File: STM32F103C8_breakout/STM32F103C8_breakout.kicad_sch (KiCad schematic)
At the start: 51 parts, among them J1 Conn1x1Pin-PA0_WKUP, J10 Conn1x1Pin-PA9, J11 Conn1x1Pin-PA10, J12 Conn1x1Pin-PA11, J13 Conn1x1Pin-PA12, J14 Conn1x1Pin-PA13, J15 Conn1x1Pin-PA14, J16 Conn1x1Pin-PA15, J17 Conn1x1Pin-PC13-TAMPER-RTC, J18 Conn1x1Pin-PC14-OSC32_IN, J19 Conn1x1Pin-PC15-OSC32_OUT, J2 Conn1x1Pin-PA1, J21 Conn_01x02_Pin, J25 Conn1x1Pin-PB15, J26 Conn1x1Pin-PB14, J27 Conn1x1Pin-PB13, J28 Conn1x1Pin-PB12, J29 Conn1x1Pin-PB11, J3 Conn1x1Pin-PA2, J30 Conn1x1Pin-PB10, J31 Conn1x1Pin-PB9, J32 Conn1x1Pin-PB8, J33 Conn1x1Pin-PB7, J34 Conn1x1Pin-PB6, J35 Conn1x1Pin-PB5, J36 Conn1x1Pin-PB4, J37 Conn1x1Pin-PB3, J38 Conn1x1Pin-PB2, J39 Conn1x1Pin-PB1, J4 Conn1x1Pin-PA3, J40 Conn1x1Pin-PB0, J5 Conn1x1Pin-PA4, J6 Conn1x1Pin-PA5, J7 Conn1x1Pin-PA6, J8 Conn1x1Pin-PA7, J9 Conn1x1Pin-PA8, U1 STM32F103C8T6, U3 GPTS203211B, Y1 6 MHz Crystal

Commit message: Worked on PCB Layout
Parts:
- removed J1: Conn1x1Pin-PA0_WKUP, Connector_PinHeader_2.54mm:PinHeader_1x01_P2.54mm_Horizontal, symbol Connector:Conn_01x01_Pin
- removed J10: Conn1x1Pin-PA9, Connector_PinHeader_2.54mm:PinHeader_1x01_P2.54mm_Horizontal, symbol Connector:Conn_01x01_Pin
- removed J11: Conn1x1Pin-PA10, Connector_PinHeader_2.54mm:PinHeader_1x01_P2.54mm_Horizontal, symbol Connector:Conn_01x01_Pin
- removed J12: Conn1x1Pin-PA11, Connector_PinHeader_2.54mm:PinHeader_1x01_P2.54mm_Horizontal, symbol Connector:Conn_01x01_Pin
- removed J13: Conn1x1Pin-PA12, Connector_PinHeader_2.54mm:PinHeader_1x01_P2.54mm_Horizontal, symbol Connector:Conn_01x01_Pin
- removed J14: Conn1x1Pin-PA13, Connector_PinHeader_2.54mm:PinHeader_1x01_P2.54mm_Horizontal, symbol Connector:Conn_01x01_Pin
- removed J15: Conn1x1Pin-PA14, Connector_PinHeader_2.54mm:PinHeader_1x01_P2.54mm_Horizontal, symbol Connector:Conn_01x01_Pin
- removed J16: Conn1x1Pin-PA15, Connector_PinHeader_2.54mm:PinHeader_1x01_P2.54mm_Horizontal, symbol Connector:Conn_01x01_Pin
- removed J17: Conn1x1Pin-PC13-TAMPER-RTC, Connector_PinHeader_2.54mm:PinHeader_1x01_P2.54mm_Horizontal, symbol Connector:Conn_01x01_Pin
- removed J18: Conn1x1Pin-PC14-OSC32_IN, Connector_PinHeader_2.54mm:PinHeader_1x01_P2.54mm_Horizontal, symbol Connector:Conn_01x01_Pin
- removed J19: Conn1x1Pin-PC15-OSC32_OUT, Connector_PinHeader_2.54mm:PinHeader_1x01_P2.54mm_Horizontal, symbol Connector:Conn_01x01_Pin
- removed J2: Conn1x1Pin-PA1, Connector_PinHeader_2.54mm:PinHeader_1x01_P2.54mm_Horizontal, symbol Connector:Conn_01x01_Pin
- removed J25: Conn1x1Pin-PB15, Connector_PinHeader_2.54mm:PinHeader_1x01_P2.54mm_Horizontal, symbol Connector:Conn_01x01_Pin
- removed J26: Conn1x1Pin-PB14, Connector_PinHeader_2.54mm:PinHeader_1x01_P2.54mm_Horizontal, symbol Connector:Conn_01x01_Pin
- removed J27: Conn1x1Pin-PB13, Connector_PinHeader_2.54mm:PinHeader_1x01_P2.54mm_Horizontal, symbol Connector:Conn_01x01_Pin
- removed J28: Conn1x1Pin-PB12, Connector_PinHeader_2.54mm:PinHeader_1x01_P2.54mm_Horizontal, symbol Connector:Conn_01x01_Pin
- removed J29: Conn1x1Pin-PB11, Connector_PinHeader_2.54mm:PinHeader_1x01_P2.54mm_Horizontal, symbol Connector:Conn_01x01_Pin
- removed J3: Conn1x1Pin-PA2, Connector_PinHeader_2.54mm:PinHeader_1x01_P2.54mm_Horizontal, symbol Connector:Conn_01x01_Pin
- removed J30: Conn1x1Pin-PB10, Connector_PinHeader_2.54mm:PinHeader_1x01_P2.54mm_Horizontal, symbol Connector:Conn_01x01_Pin
- removed J31: Conn1x1Pin-PB9, Connector_PinHeader_2.54mm:PinHeader_1x01_P2.54mm_Horizontal, symbol Connector:Conn_01x01_Pin
- removed J32: Conn1x1Pin-PB8, Connector_PinHeader_2.54mm:PinHeader_1x01_P2.54mm_Horizontal, symbol Connector:Conn_01x01_Pin
- removed J33: Conn1x1Pin-PB7, Connector_PinHeader_2.54mm:PinHeader_1x01_P2.54mm_Horizontal, symbol Connector:Conn_01x01_Pin
- removed J34: Conn1x1Pin-PB6, Connector_PinHeader_2.54mm:PinHeader_1x01_P2.54mm_Horizontal, symbol Connector:Conn_01x01_Pin
- removed J35: Conn1x1Pin-PB5, Connector_PinHeader_2.54mm:PinHeader_1x01_P2.54mm_Horizontal, symbol Connector:Conn_01x01_Pin
- removed J36: Conn1x1Pin-PB4, Connector_PinHeader_2.54mm:PinHeader_1x01_P2.54mm_Horizontal, symbol Connector:Conn_01x01_Pin
- removed J37: Conn1x1Pin-PB3, Connector_PinHeader_2.54mm:PinHeader_1x01_P2.54mm_Horizontal, symbol Connector:Conn_01x01_Pin
- removed J38: Conn1x1Pin-PB2, Connector_PinHeader_2.54mm:PinHeader_1x01_P2.54mm_Horizontal, symbol Connector:Conn_01x01_Pin
- removed J39: Conn1x1Pin-PB1, Connector_PinHeader_2.54mm:PinHeader_1x01_P2.54mm_Horizontal, symbol Connector:Conn_01x01_Pin
- removed J4: Conn1x1Pin-PA3, Connector_PinHeader_2.54mm:PinHeader_1x01_P2.54mm_Horizontal, symbol Connector:Conn_01x01_Pin
- removed J40: Conn1x1Pin-PB0, Connector_PinHeader_2.54mm:PinHeader_1x01_P2.54mm_Horizontal, symbol Connector:Conn_01x01_Pin
- removed J5: Conn1x1Pin-PA4, Connector_PinHeader_2.54mm:PinHeader_1x01_P2.54mm_Horizontal, symbol Connector:Conn_01x01_Pin
- removed J6: Conn1x1Pin-PA5, Connector_PinHeader_2.54mm:PinHeader_1x01_P2.54mm_Horizontal, symbol Connector:Conn_01x01_Pin
- removed J7: Conn1x1Pin-PA6, Connector_PinHeader_2.54mm:PinHeader_1x01_P2.54mm_Horizontal, symbol Connector:Conn_01x01_Pin
- removed J8: Conn1x1Pin-PA7, Connector_PinHeader_2.54mm:PinHeader_1x01_P2.54mm_Horizontal, symbol Connector:Conn_01x01_Pin
- removed J9: Conn1x1Pin-PA8, Connector_PinHeader_2.54mm:PinHeader_1x01_P2.54mm_Horizontal, symbol Connector:Conn_01x01_Pin
- added D1: WL-SMCC_0402, SMD_LED_GREEN:WL-SMCC_0402, symbol LED_SMD_GREEN:WL-SMCC_0402
- added J1: Conn_01x18_Pin, Connector_PinHeader_2.54mm:PinHeader_1x18_P2.54mm_Vertical, symbol Connector:Conn_01x18_Pin
- added J2: Conn_01x14_Pin, Connector_PinHeader_2.54mm:PinHeader_1x14_P2.54mm_Vertical, symbol Connector:Conn_01x14_Pin
- added R7: 10kΩ, Resistor_SMD:R_0805_2012Metric_Pad1.20x1.40mm_HandSolder, symbol Device:R_US
- J21: footprint Connector_PinHeader_1.00mm:PinHeader_1x02_P1.00mm_Horizontal -> Connector_PinHeader_2.54mm:PinHeader_1x02_P2.54mm_Vertical
- U3: footprint SWITCH_03211B -> Push_Button:SWITCH_03211B
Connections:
- net GNDREF: now also J1.5 (Pin_5), R7.1
- net VDD: now also J1.1 (Pin_1)
- net PA3: now reaches U1.13 (PA3)
- net PA3: now also J1.9 (Pin_9)
- net at C1.1, C2.1, FB1.2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: now also D1.2
- net PB9: now reaches U1.46 (PB9)
- net PB9: now also J2.1 (Pin_1)
- net PA0_WKUP: now reaches U1.10 (PA0_WKUP)
- net PA0_WKUP: now also J1.6 (Pin_6)
- net PA1: now reaches U1.11 (PA1)
- net PA1: now also J1.7 (Pin_7)
- net PA2: now reaches U1.12 (PA2)
- net PA2: now also J1.8 (Pin_8)
- net PA4: now reaches U1.14 (PA4)
- net PA4: now also J1.10 (Pin_10)
- net PA5: now reaches U1.15 (PA5)
- net PA5: now also J1.11 (Pin_11)
- net PA6: now reaches U1.16 (PA6)
- net PA6: now also J1.12 (Pin_12)
- net PA7: now reaches U1.17 (PA7)
- net PA7: now also J1.13 (Pin_13)
- net PB0: now reaches U1.18 (PB0)
- net PB0: now also J1.14 (Pin_14)
- net PB1: now reaches U1.19 (PB1)
- net PB1: now also J1.15 (Pin_15)
- net PC13: now reaches U1.2 (PC13-TAMPER-RTC)
- net PC13: now also J1.2 (Pin_2)
- net PB2: now reaches U1.20 (PB2)
- net PB2: now also J1.16 (Pin_16)
- net PB10: now reaches U1.21 (PB10)
- net PB10: now also J1.17 (Pin_17)
- net PB11: now reaches U1.22 (PB11)
- net PB11: now also J1.18 (Pin_18)
- net PB12: now reaches U1.25 (PB12)
- net PB12: now also J2.14 (Pin_14)
- net PB13: now reaches U1.26 (PB13)
- net PB13: now also J2.13 (Pin_13)
- net PB14: now reaches U1.27 (PB14)
- net PB14: now also J2.12 (Pin_12)
- net PB15: now reaches U1.28 (PB15)
- net PB15: now also J2.11 (Pin_11)
- net PA8: now reaches U1.29 (PA8)
- net PA8: now also J2.10 (Pin_10)
- net PC14: now reaches U1.3 (PC14-OSC32_IN)
- net PC14: now also J1.3 (Pin_3)
- net PA9: now reaches U1.30 (PA9)
- net PA9: now also J2.9 (Pin_9)
- net PA10: now reaches U1.31 (PA10)
- net PA10: now also J2.8 (Pin_8)
- net PA11: now reaches U1.32 (PA11)
- net PA11: now also J2.7 (Pin_7)
- net PA12: now reaches U1.33 (PA12)
- net PA12: now also J2.6 (Pin_6)
- net PC15: now reaches U1.4 (PC15-OSC32_OUT)
- net PC15: now also J1.4 (Pin_4)
- net PB5: now reaches U1.41 (PB5)
- net PB5: now also J2.5 (Pin_5)
- net PB6: now reaches U1.42 (PB6)
- net PB6: now also J2.4 (Pin_4)
- net PB7: now reaches U1.43 (PB7)
- net PB7: now also J2.3 (Pin_3)
- net PB8: now reaches U1.45 (PB8)
- net PB8: now also J2.2 (Pin_2)
- new net: D1.1, R7.2
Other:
- note added: "Power LED"

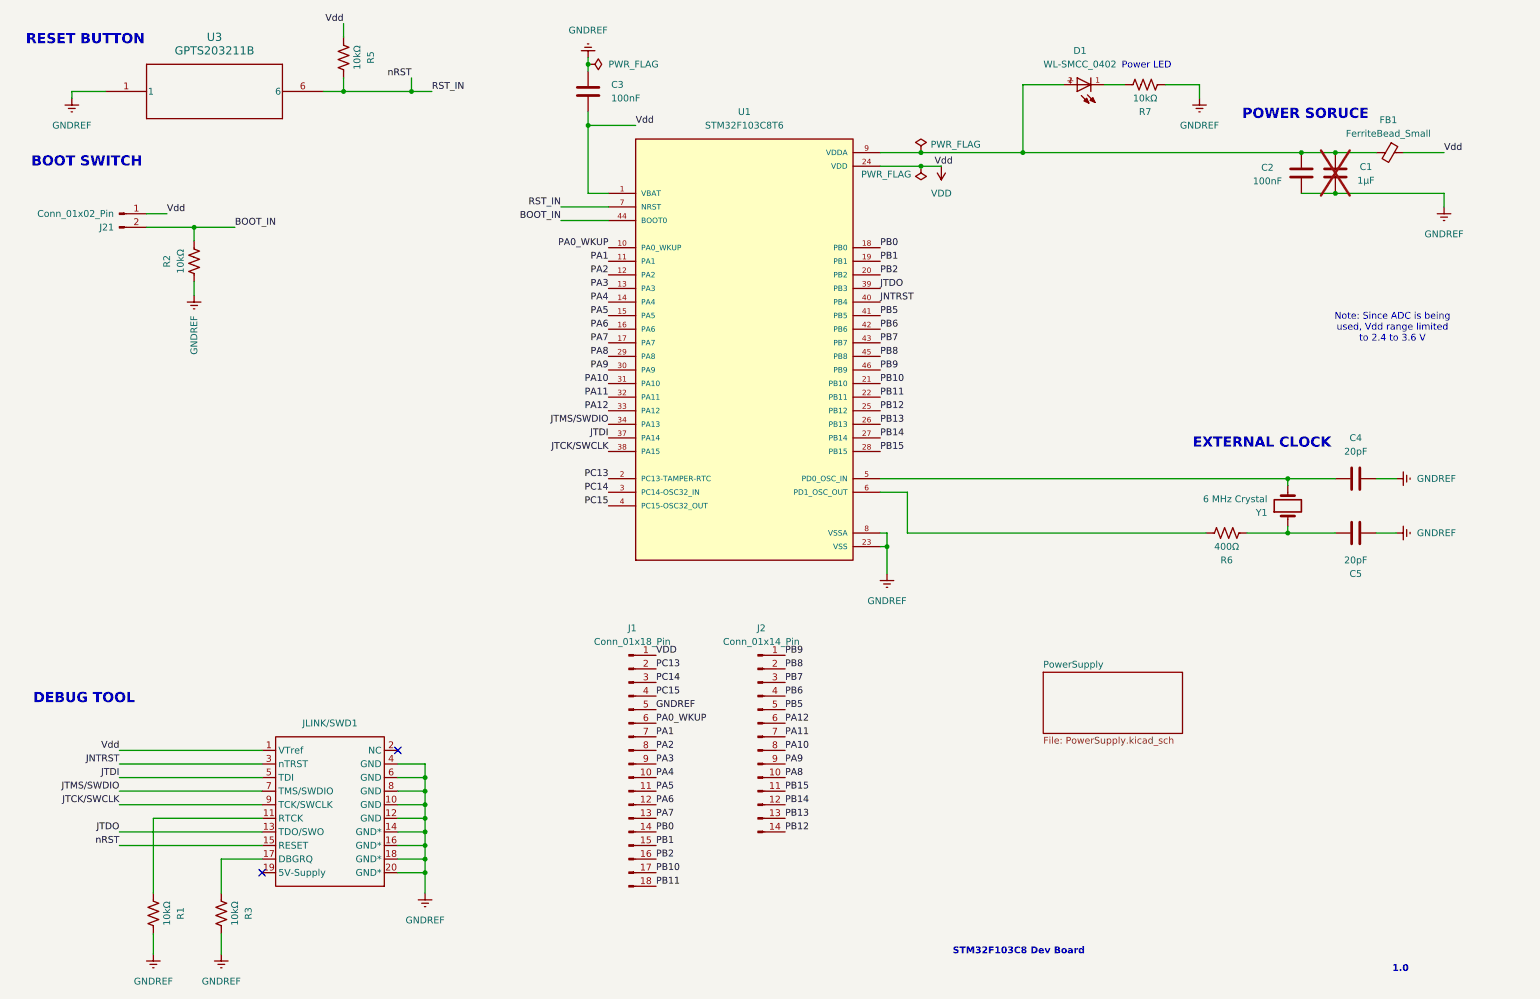
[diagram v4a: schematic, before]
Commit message: Completed PCB Layoutx
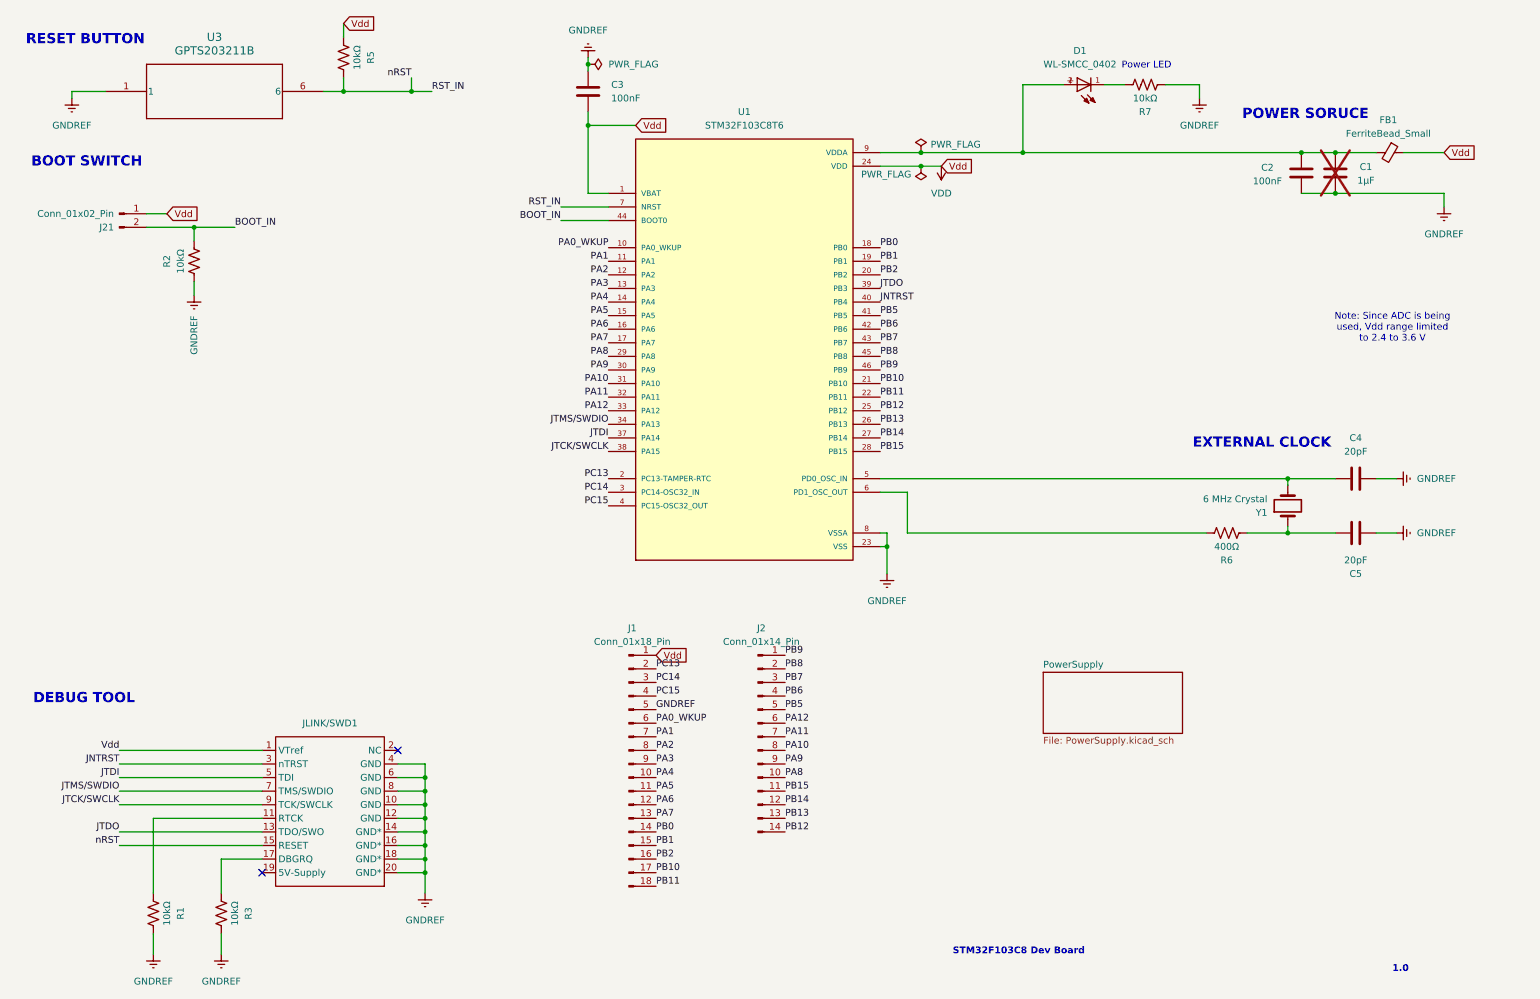
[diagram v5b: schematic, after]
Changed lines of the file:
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@@
-		)
-	)
-	(label "Vdd"
-		(at 39.37 52.07 0)
-		(effects
-			(font
-				(size 1.27 1.27)
-			)
-			(justify left bottom)
-		)
-	)
-	(label "VDD"
-		(at 130.81 134.62 0)
-		(effects
-			(font
-				(size 1.27 1.27)
-			)
-			(justify left bottom)
 		)
 	)
@@
 		)
 	)
-	(label "Vdd"
-		(at 278.13 40.64 0)
-		(effects
-			(font
-				(size 1.27 1.27)
-			)
-			(justify left bottom)
-		)
-	)
 	(label "PB14"
 		(at 154.94 162.56 0)
@@
 		)
 	)
-	(label "Vdd"
-		(at 182.88 43.18 0)
-		(effects
-			(font
-				(size 1.27 1.27)
-			)
-			(justify left bottom)
-		)
-	)
 	(label "PC14"
 		(at 121.92 104.14 180)
@@
 	)
 	(label "Vdd"
-		(at 72.39 16.51 180)
-		(effects
-			(font
-				(size 1.27 1.27)
-			)
-			(justify right bottom)
-		)
-	)
-	(label "Vdd"
 		(at 30.48 152.4 180)
 		(effects
@@
 		)
 	)
-	(label "Vdd"
-		(at 127 35.56 0)
-		(effects
-			(font
-				(size 1.27 1.27)
-			)
-			(justify left bottom)
-		)
-	)
 	(label "JNTRST"
 		(at 172.72 68.58 0)
@@
 		)
 	)
+	(global_label "Vdd"
+		(shape input)
+		(at 278.13 40.64 0)
+		(fields_autoplaced yes)
+		(effects
+			(font
+				(size 1.27 1.27)
+			)
+			(justify left)
+		)
+		(property "Intersheetrefs" "${INTERSHEET_REFS}"
+			(at 284.5018 40.64 0)
+			(hide yes)
+			(show_name no)
+			(do_not_autoplace no)
+			(effects
+				(font
+					(size 1.27 1.27)
+				)
+				(justify left)
+			)
+		)
+	)
+	(global_label "Vdd"
+		(shape input)
+		(at 72.39 16.51 0)
+		(fields_autoplaced yes)
+		(effects
+			(font
+				(size 1.27 1.27)
+			)
+			(justify left)
+		)
+		(property "Intersheetrefs" "${INTERSHEET_REFS}"
+			(at 78.7618 16.51 0)
+			(hide yes)
+			(show_name no)
+			(do_not_autoplace no)
+			(effects
+				(font
+					(size 1.27 1.27)
+				)
+				(justify left)
+			)
+		)
+	)
+	(global_label "Vdd"
+		(shape input)
+		(at 127 35.56 0)
+		(fields_autoplaced yes)
+		(effects
+			(font
+				(size 1.27 1.27)
+			)
+			(justify left)
+		)
+		(property "Intersheetrefs" "${INTERSHEET_REFS}"
+			(at 133.3718 35.56 0)
+			(hide yes)
+			(show_name no)
+			(do_not_autoplace no)
+			(effects
+				(font
+					(size 1.27 1.27)
+				)
+				(justify left)
+			)
+		)
+	)
+	(global_label "Vdd"
+		(shape input)
+		(at 39.37 52.07 0)
+		(fields_autoplaced yes)
+		(effects
+			(font
+				(size 1.27 1.27)
+			)
+			(justify left)
+		)
+		(property "Intersheetrefs" "${INTERSHEET_REFS}"
+			(at 45.7418 52.07 0)
+			(hide yes)
+			(show_name no)
+			(do_not_autoplace no)
+			(effects
+				(font
+					(size 1.27 1.27)
+				)
+				(justify left)
+			)
+		)
+	)
+	(global_label "Vdd"
+		(shape input)
+		(at 184.15 43.18 0)
+		(fields_autoplaced yes)
+		(effects
+			(font
+				(size 1.27 1.27)
+			)
+			(justify left)
+		)
+		(property "Intersheetrefs" "${INTERSHEET_REFS}"
+			(at 190.5218 43.18 0)
+			(hide yes)
+			(show_name no)
+			(do_not_autoplace no)
+			(effects
+				(font
+					(size 1.27 1.27)
+				)
+				(justify left)
+			)
+		)
+	)
+	(global_label "Vdd"
+		(shape input)
+		(at 130.81 134.62 0)
+		(fields_autoplaced yes)
+		(effects
+			(font
+				(size 1.27 1.27)
+			)
+			(justify left)
+		)
+		(property "Intersheetrefs" "${INTERSHEET_REFS}"
+			(at 137.1818 134.62 0)
+			(hide yes)
+			(show_name no)
+			(do_not_autoplace no)
+			(effects
+				(font
+					(size 1.27 1.27)
+				)
+				(justify left)
+			)
+		)
+	)

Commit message: Finalized PCB Design. Ready for Review.
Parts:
- added R8: 10kΩ, Resistor_SMD:R_0805_2012Metric_Pad1.20x1.40mm_HandSolder, symbol Device:R_US
- C1: now fitted
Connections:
- net PB2: now also R8.2
- net GNDREF renamed VSS
- net VSS: now also R8.1
